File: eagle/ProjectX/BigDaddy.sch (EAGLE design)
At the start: 180 parts, among them U10 TC4427AEOA, U11 TC4427AEOA, U12 TC4427AEOA, U13 TC4427AEOA, U19 TC4427AEOA, U20 TC4427AEOA, U21 TC4427AEOA, U22 TC4427AEOA, U23 TC4427AEOA, U24 TC4427AEOA, U25 TC4427AEOA, U26 TC4427AEOA, U27 TC4427AEOA, U28 TC4427AEOA, U29 TC4427AEOA, U3 TC4427AEOA, U30 TC4427AEOA, U31 TC4427AEOA, U32 TC4427AEOA, U34 TC4427AEOA, U35 TC4427AEOA, U36 TC4427AEOA, U37 TC4427AEOA, U38 TC4427AEOA, U39 TC4427AEOA, U4 TC4427AEOA, U40 TC4427AEOA, U41 TC4427AEOA, U42 TC4427AEOA, U43 TC4427AEOA, U44 TC4427AEOA, U45 TC4427AEOA, U5 TC4427AEOA, U55 TC4427AEOA, U56 TC4427AEOA, U57 TC4427AEOA, U58 TC4427AEOA, U59 TC4427AEOA, U60 TC4427AEOA, U61 TC4427AEOA, U62 TC4427AEOA, U63 TC4427AEOA, U7 TC4427AEOA, U9 TC4427AEOA

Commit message: More work on the board
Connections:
- new net 1: DIP1.2, U28.IN_B
- new net 2: DIP1.4, U28.IN_A
- new net 3: DIP1.3, U29.IN_B
- new net 4: DIP1.5, U29.IN_A
- new net N$1: DIP1.203, J2.1
- new net N$13: DIP1.190, J2.5
- new net N$14: DIP1.187, J2.6
- new net N$17: DIP1.185, J2.7
- new net N$18: DIP1.180, J2.8
- new net N$2: DIP1.200, J2.2
- new net N$29: DIP1.178, J2.9
- new net N$3: DIP1.197, J2.3
- new net N$30: DIP1.172, J2.10
- new net N$4: DIP1.193, J2.4
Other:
- moved on the sheet: J2
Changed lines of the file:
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@@
 <instance part="GND61" gate="1" x="-149.86" y="35.56" rot="R180"/>
 <instance part="GND62" gate="1" x="-104.14" y="38.1" rot="R180"/>
-<instance part="SUPPLY31" gate="VDD" x="-96.52" y="27.94" rot="R270"/>
+<instance part="SUPPLY31" gate="VDD" x="-101.6" y="27.94" rot="R270"/>
 <instance part="C29" gate="G$1" x="-101.6" y="33.02"/>
 <instance part="SP59" gate="G$1" x="40.64" y="45.72" rot="MR180"/>
@@
 <instance part="SUPPLY4" gate="VDD" x="353.06" y="-101.6"/>
 <instance part="SUPPLY8" gate="+5V" x="373.38" y="-99.06"/>
-<instance part="J2" gate="G$1" x="210.82" y="33.02" rot="R270"/>
+<instance part="J2" gate="G$1" x="210.82" y="25.4" rot="R270"/>
 </instances>
 <busses>
+<bus name="1,2,3,4,5,6,7,8,9,10,11,12,13,14,15,16,17,18,19,20,21,22,23,24,25,26,27,28,29,30,31,32,33,34,35,36,37,38,39,40,41,42,43,44,45,46,47,48,49,50,51,52,53,54,55,56,57,58,59,60,61,62,63,64,65,66,67,68,69,70,71,72,73,74,75,76,77,78,79,80,81,82,83,84,85,86,87,88">
+<segment>
+<wire x1="142.24" y1="78.74" x2="-162.56" y2="78.74" width="0.762" layer="92"/>
+<wire x1="-162.56" y1="78.74" x2="-162.56" y2="7.62" width="0.762" layer="92"/>
+<wire x1="-162.56" y1="7.62" x2="137.16" y2="7.62" width="0.762" layer="92"/>
+<wire x1="-162.56" y1="7.62" x2="-162.56" y2="-50.8" width="0.762" layer="92"/>
+<wire x1="-162.56" y1="-50.8" x2="137.16" y2="-50.8" width="0.762" layer="92"/>
+<wire x1="-162.56" y1="-50.8" x2="-162.56" y2="-106.68" width="0.762" layer="92"/>
+<wire x1="-162.56" y1="-106.68" x2="139.7" y2="-106.68" width="0.762" layer="92"/>
+<wire x1="-162.56" y1="-106.68" x2="-162.56" y2="-170.18" width="0.762" layer="92"/>
+<wire x1="-162.56" y1="-170.18" x2="142.24" y2="-170.18" width="0.762" layer="92"/>
+<wire x1="-162.56" y1="-170.18" x2="-162.56" y2="-220.98" width="0.762" layer="92"/>
+<wire x1="-162.56" y1="-220.98" x2="167.64" y2="-220.98" width="0.762" layer="92"/>
+<wire x1="167.64" y1="-220.98" x2="167.64" y2="-22.86" width="0.762" layer="92"/>
+<wire x1="167.64" y1="-22.86" x2="226.06" y2="-22.86" width="0.762" layer="92"/>
+<wire x1="226.06" y1="-22.86" x2="226.06" y2="-99.06" width="0.762" layer="92"/>
+<wire x1="226.06" y1="-22.86" x2="279.4" y2="-22.86" width="0.762" layer="92"/>
+<wire x1="279.4" y1="-22.86" x2="279.4" y2="-99.06" width="0.762" layer="92"/>
+<wire x1="167.64" y1="-22.86" x2="167.64" y2="15.24" width="0.762" layer="92"/>
+<wire x1="167.64" y1="15.24" x2="190.5" y2="15.24" width="0.762" layer="92"/>
+</segment>
+</bus>
 </busses>
 <nets>
@@
 <pinref part="SUPPLY31" gate="VDD" pin="VDD"/>
 <pinref part="C29" gate="G$1" pin="2"/>
-<wire x1="-101.6" y1="27.94" x2="-96.52" y2="27.94" width="0.1524" layer="91"/>
 <junction x="-101.6" y="27.94"/>
 </segment>
@@
 </segment>
 </net>
+<net name="N$1" class="0">
+<segment>
+<pinref part="J2" gate="G$1" pin="1"/>
+<pinref part="DIP1" gate="G$1" pin="203"/>
+<wire x1="193.04" y1="15.24" x2="193.04" y2="10.16" width="0.1524" layer="91"/>
+</segment>
+</net>
+<net name="N$2" class="0">
+<segment>
+<pinref part="J2" gate="G$1" pin="2"/>
+<pinref part="DIP1" gate="G$1" pin="200"/>
+<wire x1="195.58" y1="15.24" x2="195.58" y2="10.16" width="0.1524" layer="91"/>
+</segment>
+</net>
+<net name="N$3" class="0">
+<segment>
+<pinref part="J2" gate="G$1" pin="3"/>
+<pinref part="DIP1" gate="G$1" pin="197"/>
+<wire x1="198.12" y1="15.24" x2="198.12" y2="10.16" width="0.1524" layer="91"/>
+</segment>
+</net>
+<net name="N$4" class="0">
+<segment>
+<pinref part="J2" gate="G$1" pin="4"/>
+<pinref part="DIP1" gate="G$1" pin="193"/>
+<wire x1="200.66" y1="15.24" x2="200.66" y2="10.16" width="0.1524" layer="91"/>
+</segment>
+</net>
+<net name="N$13" class="0">
+<segment>
+<pinref part="J2" gate="G$1" pin="5"/>
+<pinref part="DIP1" gate="G$1" pin="190"/>
+<wire x1="203.2" y1="15.24" x2="203.2" y2="10.16" width="0.1524" layer="91"/>
+</segment>
+</net>
+<net name="N$14" class="0">
+<segment>
+<pinref part="J2" gate="G$1" pin="6"/>
+<pinref part="DIP1" gate="G$1" pin="187"/>
+<wire x1="205.74" y1="15.24" x2="205.74" y2="10.16" width="0.1524" layer="91"/>
+</segment>
+</net>
+<net name="N$17" class="0">
+<segment>
+<pinref part="J2" gate="G$1" pin="7"/>
+<pinref part="DIP1" gate="G$1" pin="185"/>
+<wire x1="208.28" y1="15.24" x2="208.28" y2="10.16" width="0.1524" layer="91"/>
+</segment>
+</net>
+<net name="N$18" class="0">
+<segment>
+<pinref part="J2" gate="G$1" pin="8"/>
+<pinref part="DIP1" gate="G$1" pin="180"/>
+<wire x1="210.82" y1="15.24" x2="210.82" y2="10.16" width="0.1524" layer="91"/>
+</segment>
+</net>
+<net name="N$29" class="0">
+<segment>
+<pinref part="J2" gate="G$1" pin="9"/>
+<pinref part="DIP1" gate="G$1" pin="178"/>
+<wire x1="213.36" y1="15.24" x2="213.36" y2="10.16" width="0.1524" layer="91"/>
+</segment>
+</net>
+<net name="N$30" class="0">
+<segment>
+<pinref part="J2" gate="G$1" pin="10"/>
+<pinref part="DIP1" gate="G$1" pin="172"/>
+<wire x1="215.9" y1="15.24" x2="215.9" y2="10.16" width="0.1524" layer="91"/>
+</segment>
+</net>
+<net name="1" class="0">
+<segment>
+<pinref part="U28" gate="A" pin="IN_B"/>
+<wire x1="-104.14" y1="48.26" x2="-88.9" y2="48.26" width="0.1524" layer="91"/>
+<wire x1="-88.9" y1="48.26" x2="-88.9" y2="78.74" width="0.1524" layer="91"/>
+</segment>
+<segment>
+<pinref part="DIP1" gate="G$1" pin="2"/>
+<wire x1="190.5" y1="10.16" x2="190.5" y2="15.24" width="0.1524" layer="91"/>
+</segment>
+</net>
+<net name="2" class="0">
+<segment>
+<pinref part="U28" gate="A" pin="IN_A"/>
+<wire x1="-104.14" y1="45.72" x2="-86.36" y2="45.72" width="0.1524" layer="91"/>
+<wire x1="-86.36" y1="45.72" x2="-86.36" y2="78.74" width="0.1524" layer="91"/>
+</segment>
+<segment>
+<pinref part="DIP1" gate="G$1" pin="4"/>
+<wire x1="187.96" y1="10.16" x2="187.96" y2="15.24" width="0.1524" layer="91"/>
+</segment>
+</net>
+<net name="3" class="0">
+<segment>
+<wire x1="-83.82" y1="78.74" x2="-83.82" y2="43.18" width="0.1524" layer="91"/>
+<wire x1="-83.82" y1="43.18" x2="-96.52" y2="43.18" width="0.1524" layer="91"/>
+<pinref part="U29" gate="A" pin="IN_B"/>
+<wire x1="-96.52" y1="43.18" x2="-96.52" y2="25.4" width="0.1524" layer="91"/>
+<wire x1="-96.52" y1="25.4" x2="-104.14" y2="25.4" width="0.1524" layer="91"/>
+</segment>
+<segment>
+<pinref part="DIP1" gate="G$1" pin="3"/>
+<wire x1="190.5" y1="-10.16" x2="190.5" y2="-22.86" width="0.1524" layer="91"/>
+</segment>
+</net>
+<net name="4" class="0">
+<segment>
+<wire x1="-81.28" y1="78.74" x2="-81.28" y2="40.64" width="0.1524" layer="91"/>
+<wire x1="-81.28" y1="40.64" x2="-93.98" y2="40.64" width="0.1524" layer="91"/>
+<pinref part="U29" gate="A" pin="IN_A"/>
+<wire x1="-93.98" y1="40.64" x2="-93.98" y2="22.86" width="0.1524" layer="91"/>
+<wire x1="-93.98" y1="22.86" x2="-104.14" y2="22.86" width="0.1524" layer="91"/>
+</segment>
+<segment>
+<pinref part="DIP1" gate="G$1" pin="5"/>
+<wire x1="187.96" y1="-10.16" x2="187.96" y2="-22.86" width="0.1524" layer="91"/>
+</segment>
+</net>

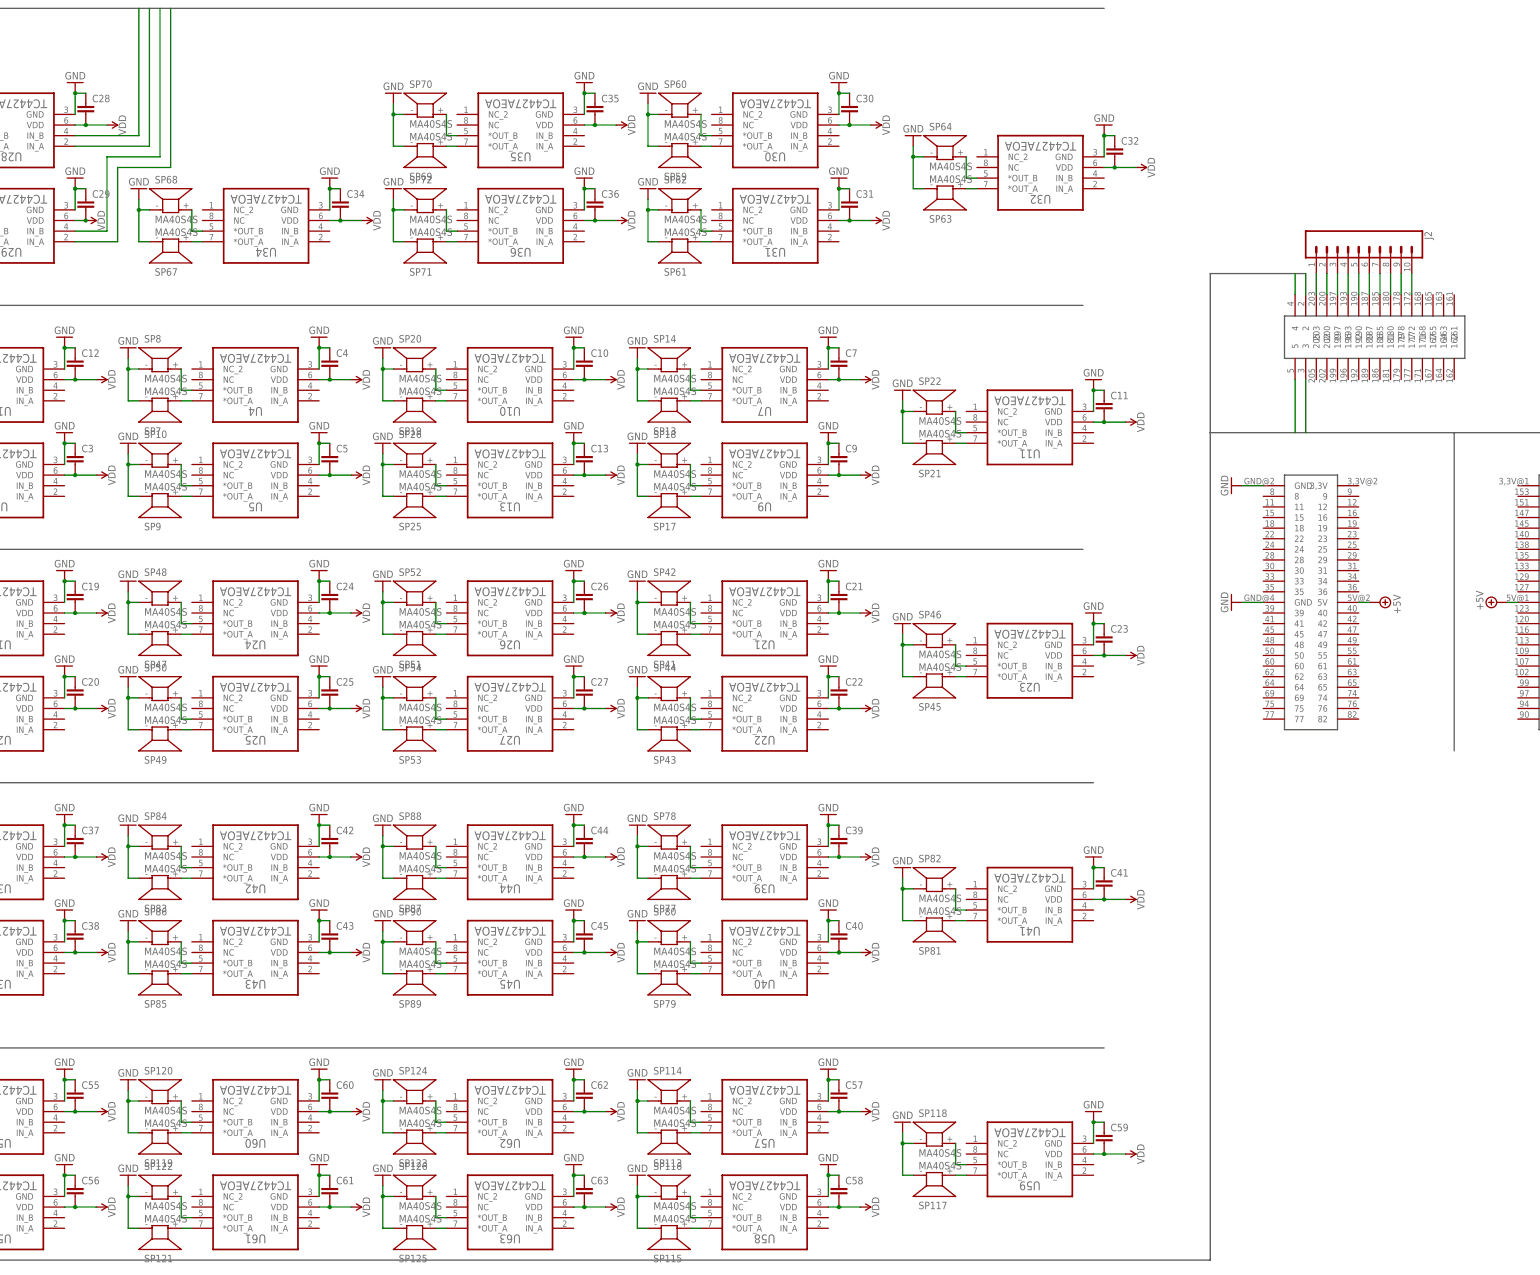
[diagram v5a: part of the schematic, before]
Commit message: Routed 16 channels
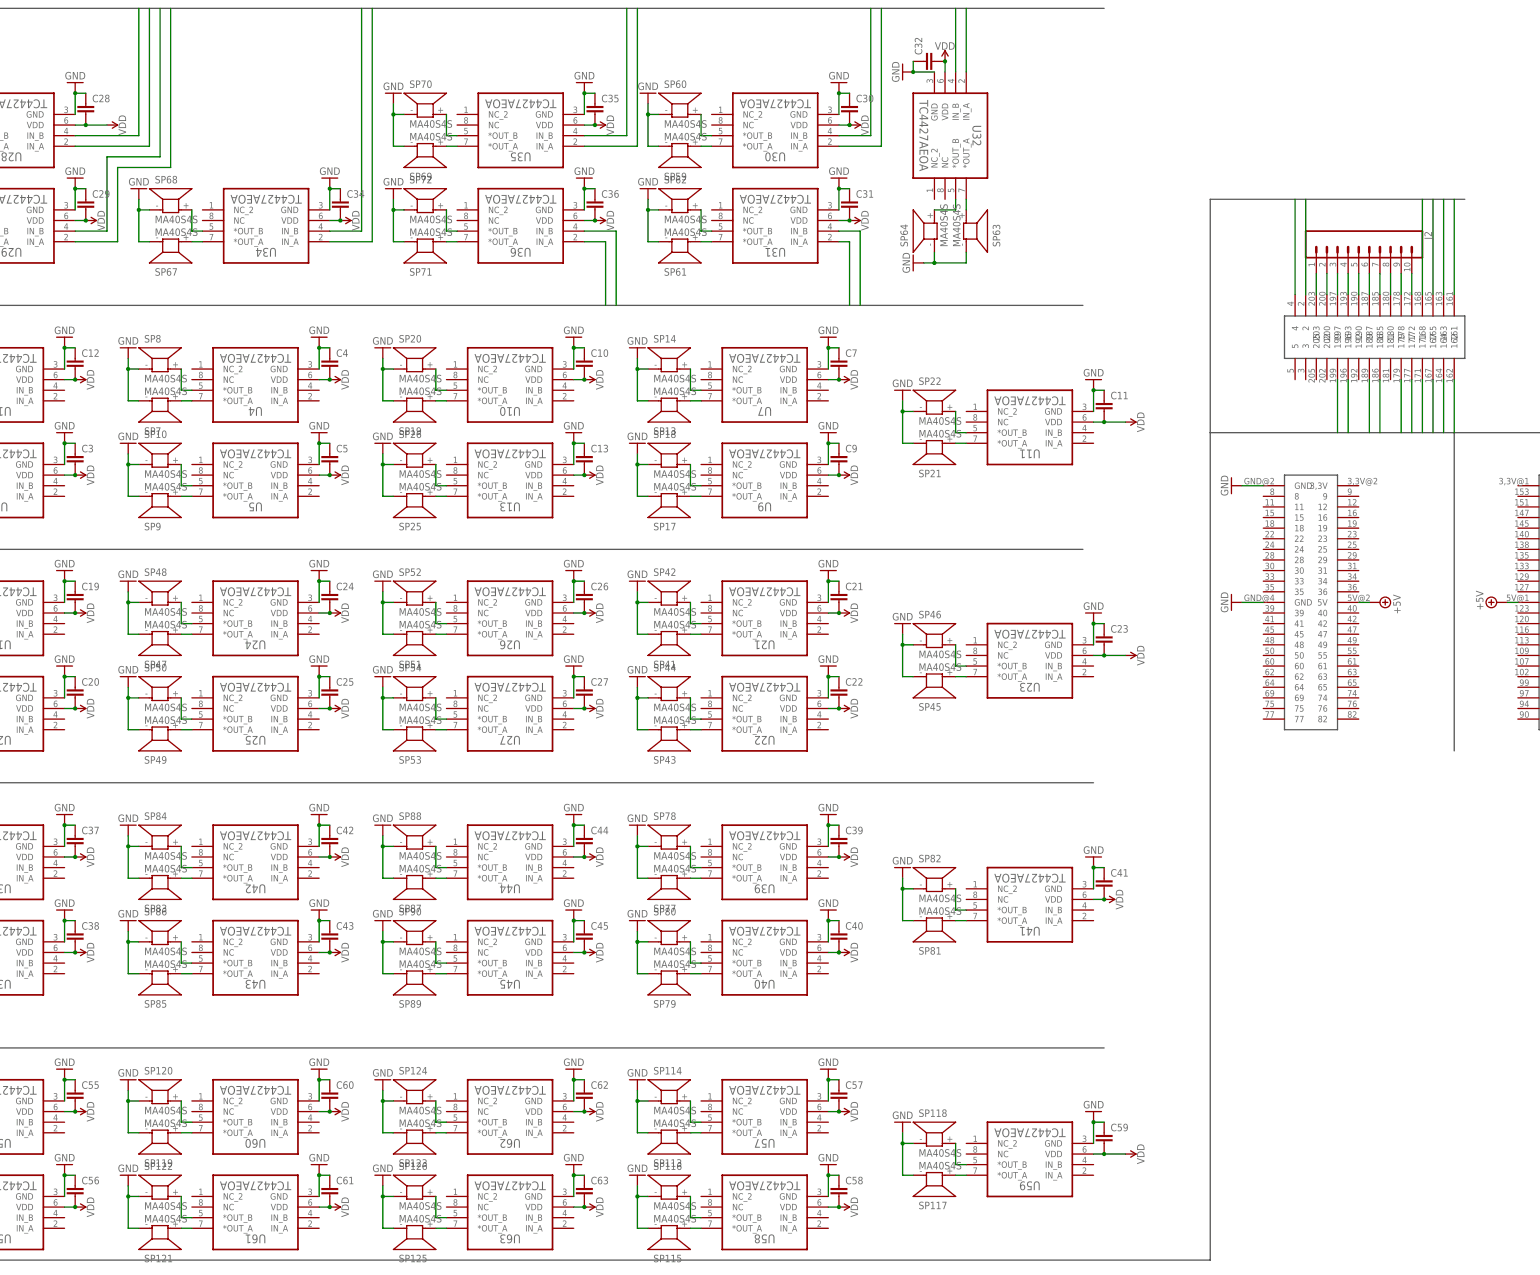
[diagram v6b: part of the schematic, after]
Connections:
- new net 10: DIP1.189, U34.IN_B
- new net 11: DIP1.186, U34.IN_A
- new net 12: DIP1.177, U36.IN_B
- new net 13: DIP1.179, U36.IN_A
- new net 14: DIP1.171, U31.IN_B
- new net 15: DIP1.167, U31.IN_A
- new net 16: DIP1.164, U32.IN_B
- new net 5: DIP1.163, U30.IN_B
- new net 6: DIP1.161, U30.IN_A
- new net 7: DIP1.162, U32.IN_A
- new net 8: DIP1.196, U29.IN_B
- new net 9: DIP1.199, U29.IN_A
- net 3: now also DIP1.165, U35.IN_B; no longer DIP1.3, U29.IN_B
- net 4: now also DIP1.168, U35.IN_A; no longer DIP1.5, U29.IN_A
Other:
- moved on the sheet: C32, SP63, SP64, U32
